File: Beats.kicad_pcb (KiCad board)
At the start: 2 copper layers, 60 x 106.5 mm, 117 parts, among them J1 AudioJack2_SwitchT, J10 AudioJack2_SwitchT, J11 AudioJack2_SwitchT, J12 AudioJack2_SwitchT, J13 AudioJack2_SwitchT, J14 AudioJack2_SwitchT, J15 AudioJack2_SwitchT, J16 AudioJack2_SwitchT, J17 Conn_02x05_Odd_Even, J18 UART, J2 AudioJack2_SwitchT, J3 AudioJack2_SwitchT, J4 AudioJack2_SwitchT, J5 AudioJack2_SwitchT, J6 AudioJack2_SwitchT, J7 SWD, J8 Conn_01x03_Male, J9 AudioJack2_SwitchT, Q1 BC847, Q10 BC847, Q11 BC847, Q12 BC847, Q13 BC847, Q2 BC847, Q3 BC847, Q4 BC847, Q5 BC847, Q6 BC847, Q7 BC847, Q8 BC847, Q9 BC847, SW1 Rotary_Encoder_Switch, SW10 SW_Push_LED, SW11 SW_Push_LED, SW12 SW_Push_LED, SW13 SW_Push_LED, SW2 SW_Push, SW3 SW_Push_LED, SW4 SW_Push_LED, SW5 SW_Push_LED, SW6 SW_Push_LED, SW7 SW_Push_LED, SW8 SW_Push_LED, SW9 SW_Push_LED, U1 MCP6004, U2 IPS240x240, U3 STM32F051R8Tx, U4 AT25xxx, U5 74AHCT244, U6 L7805, U7 LM1117-3.3, Y1 8MHz

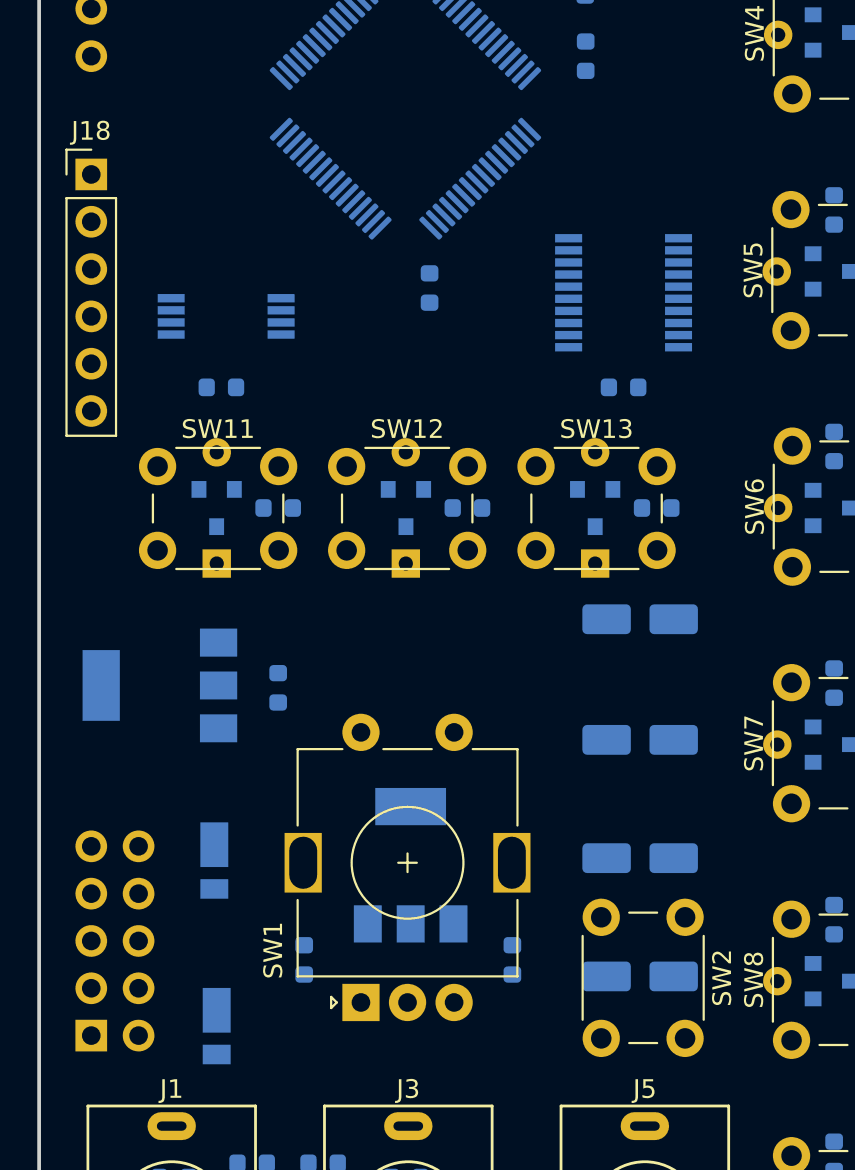
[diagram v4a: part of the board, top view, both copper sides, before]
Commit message: Correct placement of reset switch.
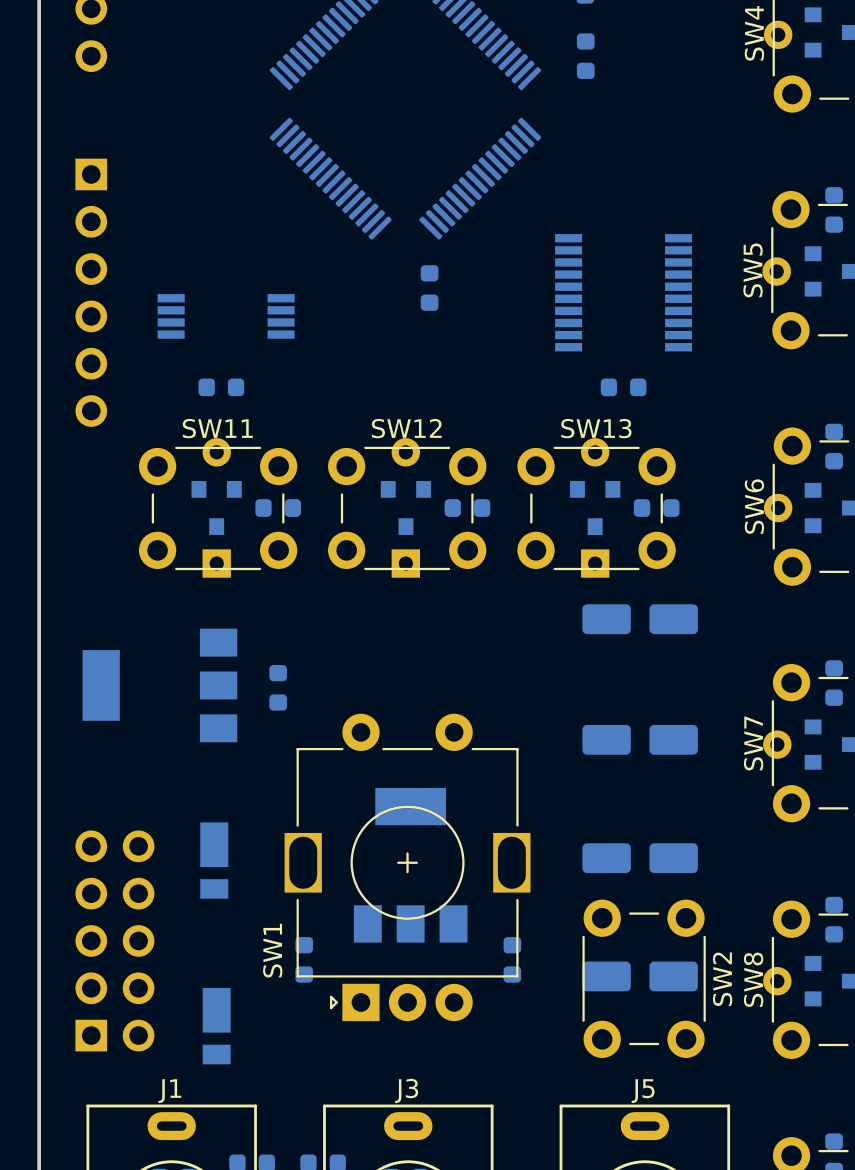
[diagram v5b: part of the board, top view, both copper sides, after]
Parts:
- J18: moved to B.Cu
- moved SW2 0.07 mm to (154.6, 115.8)
- turned J18 to 180 degrees
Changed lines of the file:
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@@
   (general
     (thickness 1.6)
-    (drawings 84)
+    (drawings 89)
     (tracks 0)
     (zones 0)
@@
     (add_net VRef-10)
   )
-  (module Connector_PinHeader_2.54mm:PinHeader_1x06_P2.54mm_Vertical (layer F.Cu)
-    (at 122.695 75.87)
+  (module Connector_PinHeader_2.54mm:PinHeader_1x06_P2.54mm_Vertical (layer B.Cu)
+    (at 122.695 75.87 180)
     (descr "Through hole straight pin header, 1x06, 2.54mm pitch, single row")
     (tags "Through hole pin header THT 1x06 2.54mm single row")
-    (fp_text reference J18 (at 0 -2.33) (layer F.SilkS)
-      (effects (font (size 1 1) (thickness 0.15)))
+    (fp_text reference J18 (at 0 2.33 180) (layer B.SilkS)
+      (effects (font (size 1 1) (thickness 0.15)) (justify mirror))
     )
-    (fp_text value UART (at 0 15.03) (layer F.Fab)
-      (effects (font (size 1 1) (thickness 0.15)))
+    (fp_text value UART (at 0 -15.03 180) (layer B.Fab)
+      (effects (font (size 1 1) (thickness 0.15)) (justify mirror))
     )
-    (fp_text user %R (at 0 6.35 90) (layer F.Fab)
-      (effects (font (size 1 1) (thickness 0.15)))
+    (fp_text user %R (at 0 -6.35 90) (layer B.Fab)
+      (effects (font (size 1 1) (thickness 0.15)) (justify mirror))
     )
-    (fp_line (start 1.8 -1.8) (end -1.8 -1.8) (layer F.CrtYd) (width 0.05))
-    (fp_line (start 1.8 14.5) (end 1.8 -1.8) (layer F.CrtYd) (width 0.05))
-    (fp_line (start -1.8 14.5) (end 1.8 14.5) (layer F.CrtYd) (width 0.05))
-    (fp_line (start -1.8 -1.8) (end -1.8 14.5) (layer F.CrtYd) (width 0.05))
-    (fp_line (start -1.33 -1.33) (end 0 -1.33) (layer F.SilkS) (width 0.12))
-    (fp_line (start -1.33 0) (end -1.33 -1.33) (layer F.SilkS) (width 0.12))
-    (fp_line (start -1.33 1.27) (end 1.33 1.27) (layer F.SilkS) (width 0.12))
-    (fp_line (start 1.33 1.27) (end 1.33 14.03) (layer F.SilkS) (width 0.12))
-    (fp_line (start -1.33 1.27) (end -1.33 14.03) (layer F.SilkS) (width 0.12))
-    (fp_line (start -1.33 14.03) (end 1.33 14.03) (layer F.SilkS) (width 0.12))
-    (fp_line (start -1.27 -0.635) (end -0.635 -1.27) (layer F.Fab) (width 0.1))
-    (fp_line (start -1.27 13.97) (end -1.27 -0.635) (layer F.Fab) (width 0.1))
-    (fp_line (start 1.27 13.97) (end -1.27 13.97) (layer F.Fab) (width 0.1))
-    (fp_line (start 1.27 -1.27) (end 1.27 13.97) (layer F.Fab) (width 0.1))
-    (fp_line (start -0.635 -1.27) (end 1.27 -1.27) (layer F.Fab) (width 0.1))
-    (pad 6 thru_hole oval (at 0 12.7) (size 1.7 1.7) (drill 1) (layers *.Cu *.Mask)
+    (fp_line (start 1.8 1.8) (end -1.8 1.8) (layer B.CrtYd) (width 0.05))
+    (fp_line (start 1.8 -14.5) (end 1.8 1.8) (layer B.CrtYd) (width 0.05))
+    (fp_line (start -1.8 -14.5) (end 1.8 -14.5) (layer B.CrtYd) (width 0.05))
+    (fp_line (start -1.8 1.8) (end -1.8 -14.5) (layer B.CrtYd) (width 0.05))
+    (fp_line (start -1.33 1.33) (end 0 1.33) (layer B.SilkS) (width 0.12))
+    (fp_line (start -1.33 0) (end -1.33 1.33) (layer B.SilkS) (width 0.12))
+    (fp_line (start -1.33 -1.27) (end 1.33 -1.27) (layer B.SilkS) (width 0.12))
+    (fp_line (start 1.33 -1.27) (end 1.33 -14.03) (layer B.SilkS) (width 0.12))
+    (fp_line (start -1.33 -1.27) (end -1.33 -14.03) (layer B.SilkS) (width 0.12))
+    (fp_line (start -1.33 -14.03) (end 1.33 -14.03) (layer B.SilkS) (width 0.12))
+    (fp_line (start -1.27 0.635) (end -0.635 1.27) (layer B.Fab) (width 0.1))
+    (fp_line (start -1.27 -13.97) (end -1.27 0.635) (layer B.Fab) (width 0.1))
+    (fp_line (start 1.27 -13.97) (end -1.27 -13.97) (layer B.Fab) (width 0.1))
+    (fp_line (start 1.27 1.27) (end 1.27 -13.97) (layer B.Fab) (width 0.1))
+    (fp_line (start -0.635 1.27) (end 1.27 1.27) (layer B.Fab) (width 0.1))
+    (pad 6 thru_hole oval (at 0 -12.7 180) (size 1.7 1.7) (drill 1) (layers *.Cu *.Mask)
       (net 150 "Net-(J18-Pad6)"))
-    (pad 5 thru_hole oval (at 0 10.16) (size 1.7 1.7) (drill 1) (layers *.Cu *.Mask)
+    (pad 5 thru_hole oval (at 0 -10.16 180) (size 1.7 1.7) (drill 1) (layers *.Cu *.Mask)
       (net 77 PA9))
-    (pad 4 thru_hole oval (at 0 7.62) (size 1.7 1.7) (drill 1) (layers *.Cu *.Mask)
+    (pad 4 thru_hole oval (at 0 -7.62 180) (size 1.7 1.7) (drill 1) (layers *.Cu *.Mask)
       (net 76 PA10))
-    (pad 3 thru_hole oval (at 0 5.08) (size 1.7 1.7) (drill 1) (layers *.Cu *.Mask)
+    (pad 3 thru_hole oval (at 0 -5.08 180) (size 1.7 1.7) (drill 1) (layers *.Cu *.Mask)
       (net 151 "Net-(J18-Pad3)"))
-    (pad 2 thru_hole oval (at 0 2.54) (size 1.7 1.7) (drill 1) (layers *.Cu *.Mask)
+    (pad 2 thru_hole oval (at 0 -2.54 180) (size 1.7 1.7) (drill 1) (layers *.Cu *.Mask)
       (net 152 "Net-(J18-Pad2)"))
-    (pad 1 thru_hole rect (at 0 0) (size 1.7 1.7) (drill 1) (layers *.Cu *.Mask)
+    (pad 1 thru_hole rect (at 0 0 180) (size 1.7 1.7) (drill 1) (layers *.Cu *.Mask)
       (net 9 GND))
     (model ${KISYS3DMOD}/Connector_PinHeader_2.54mm.3dshapes/PinHeader_1x06_P2.54mm_Vertical.wrl
@@
     )
   )
-  (module Button_Switch_THT:SW_PUSH_6mm (layer F.Cu)
-    (at 154.572 115.748 270)
+  (module Button_Switch_THT:SW_PUSH_6mm locked (layer F.Cu)
+    (at 154.6228 115.7988 270)
     (descr https://www.omron.com/ecb/products/pdf/en-b3f.pdf)
     (tags "tact sw push 6mm")
@@
     )
   )
+  (gr_circle (center 152.337234 119.05) (end 153.837234 119.05) (layer Dwgs.User) (width 0.2))
+  (gr_line (start 162.574999 119.05) (end 152.337234 119.05) (layer Dwgs.User) (width 0.2))
   (gr_line (start 125.715 69.150367) (end 153.715 69.150367) (layer Dwgs.User) (width 0.2))
   (gr_line (start 139.715 49.540367) (end 139.715 88.760367) (layer Dwgs.User) (width 0.2))
@@
   (gr_circle (center 139.715 144.45) (end 142.815 144.45) (layer Dwgs.User) (width 0.2))
   (gr_circle (center 127.015 144.45) (end 130.115 144.45) (layer Dwgs.User) (width 0.2))
-  (gr_line (start 179.733999 144.45) (end 119.774 144.45) (layer Dwgs.User) (width 0.2))
+  (gr_line (start 179.854999 144.45) (end 119.895 144.45) (layer Dwgs.User) (width 0.2))
   (gr_line (start 139.715 100) (end 139.715 164.25) (layer Dwgs.User) (width 0.2))
   (gr_line (start 127.015 99.999999) (end 127.015 164.25) (layer Dwgs.User) (width 0.2))
@@
   (gr_line (start 119.395 35.749999) (end 119.395 164.25) (layer Dwgs.User) (width 0.2))
   (gr_line (start 180.354999 35.75) (end 119.395 35.749999) (layer Dwgs.User) (width 0.2))
+  (gr_line (start 139.715 49.540367) (end 139.715 88.760367) (layer Dwgs.User) (width 0.2))
+  (gr_line (start 125.715 49.540367) (end 125.715 88.760367) (layer Dwgs.User) (width 0.2))
+  (gr_line (start 153.715 49.540367) (end 125.715 49.540367) (layer Dwgs.User) (width 0.2))
   (gr_line (start 179.854999 153.25) (end 179.854999 46.749999) (layer Edge.Cuts) (width 0.2))
   (gr_line (start 119.894999 153.25) (end 179.854999 153.25) (layer Edge.Cuts) (width 0.2))

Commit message: Assigned led and switch pins.
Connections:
- Q10 pad 1: /sheet5DB3CABC/LED -> PF7
- Q3 pad 1: /PushLED/LED -> PC13
- Q4 pad 1: /sheet5DAF110B/LED -> PC15
- Q5 pad 1: /sheet5DB16B82/LED -> PC1
- Q6 pad 1: /sheet5DB16B86/LED -> PC3
- Q7 pad 1: /sheet5DB3CAB0/LED -> PA1
- Q8 pad 1: /sheet5DB3CAB4/LED -> PC11
- Q9 pad 1: /sheet5DB3CAB8/LED -> PA15
- SW10 pad 1: /sheet5DB3CABC/SW -> PF6
- SW3 pad 1: /PushLED/SW -> PC14
- SW4 pad 1: /sheet5DAF110B/SW -> PC0
- SW5 pad 1: /sheet5DB16B82/SW -> PC2
- SW6 pad 1: /sheet5DB16B86/SW -> PA0
- SW7 pad 1: /sheet5DB3CAB0/SW -> PA2
- SW8 pad 1: /sheet5DB3CAB4/SW -> PC10
- SW9 pad 1: /sheet5DB3CAB8/SW -> PA12
- U2 pad 5: Net-(U2-Pad5) -> PC12
- U2 pad 6: Net-(U2-Pad6) -> PB4
- U2 pad 7: Net-(U2-Pad7) -> PD2
